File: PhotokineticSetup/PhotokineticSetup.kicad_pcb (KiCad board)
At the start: 2 copper layers, 26 parts, among them J1 Conn_01x02, J2 Serial, J3 LEDs, J4 Switches, J5 Outputs, J6 Inputs, J7 Conn_01x20, J8 Conn_01x20, U1 MAX232, U2 ILD615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

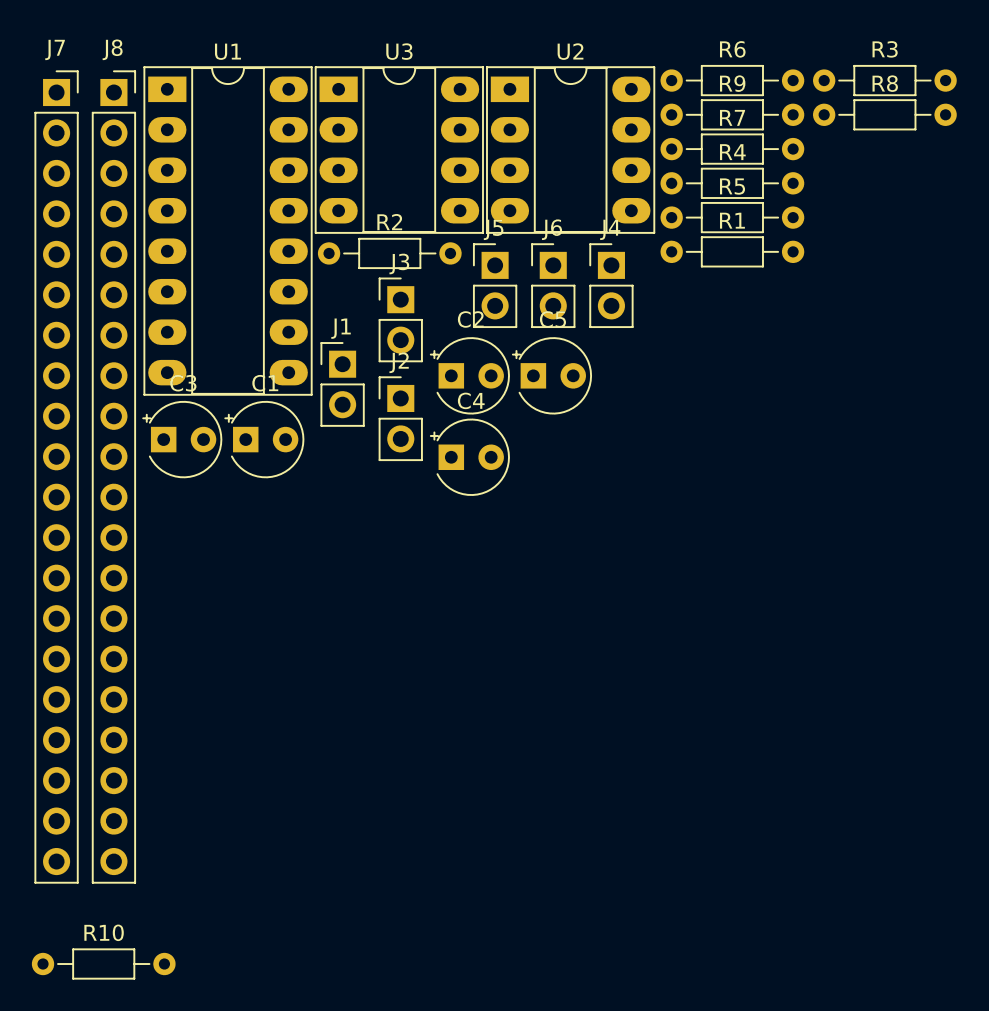
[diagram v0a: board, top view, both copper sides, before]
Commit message: Clearer optocouplers outputs and stronger input
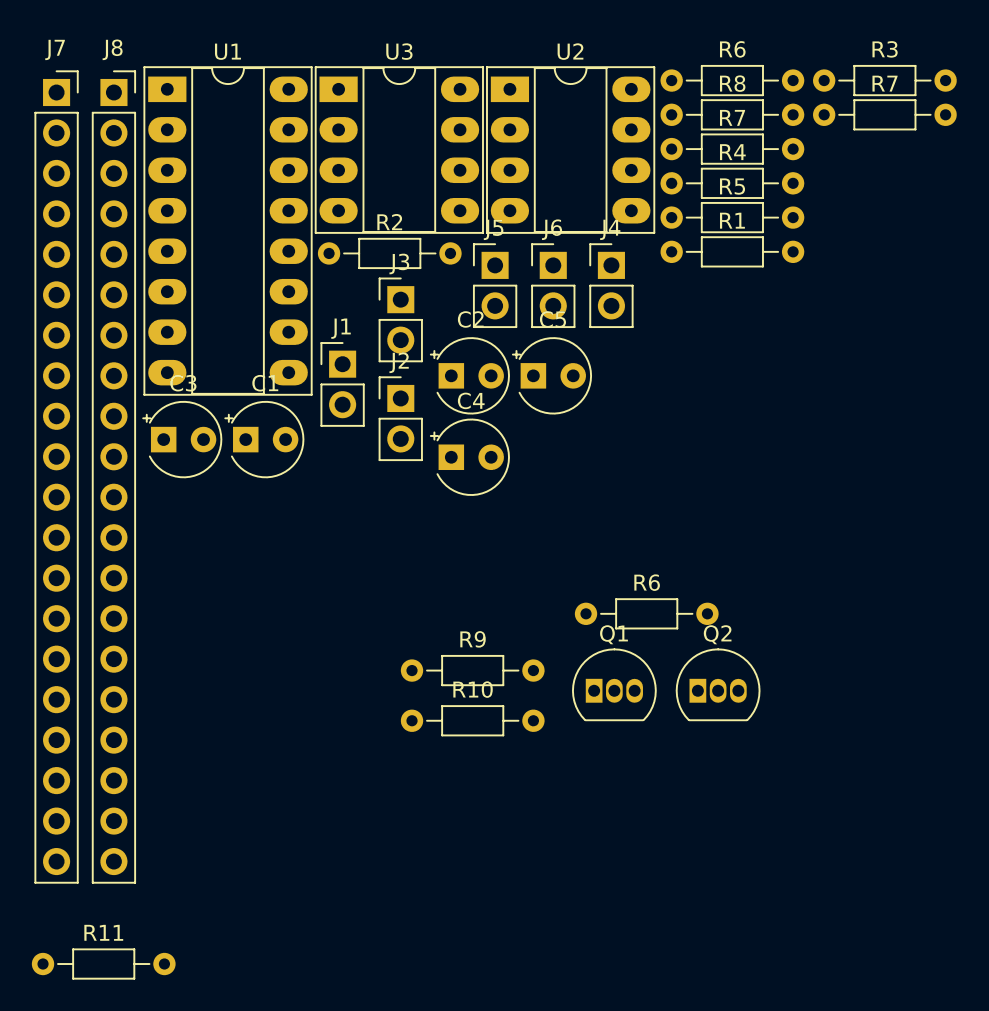
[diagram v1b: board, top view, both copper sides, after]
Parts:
- added Q1: 2N3904, Package_TO_SOT_THT:TO-92_Inline, F.Cu at (124.5, 99.1)
- added Q2: 2N3904, Package_TO_SOT_THT:TO-92_Inline, F.Cu at (131.0, 99.1)
- added R10: 1k, Resistor_THT:R_Axial_DIN0204_L3.6mm_D1.6mm_P7.62mm_Horizontal, F.Cu at (113.0, 100.9)
- added R6: 1k, Resistor_THT:R_Axial_DIN0204_L3.6mm_D1.6mm_P7.62mm_Horizontal, F.Cu at (124.0, 94.2)
- added R9: 1k, Resistor_THT:R_Axial_DIN0204_L3.6mm_D1.6mm_P7.62mm_Horizontal, F.Cu at (113.0, 97.8)
- renumbered R10 to R11, R8 to R7, R9 to R8
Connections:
- J8 pad 13: Net-(J8-Pad13) -> /PA3
- J8 pad 14: Net-(J8-Pad14) -> /PA2
- R5 pad 2: Net-(R5-Pad2) -> Net-(J5-Pad1)
- R7 pad 1: Net-(J6-Pad1) -> +3V3
- R8 pad 1: Net-(J6-Pad2) -> +3V3
- U1 pad 10: Net-(U1-Pad10) -> /PA2
- U1 pad 15: GND -> Net-(U1-Pad15)
- U1 pad 9: Net-(U1-Pad9) -> /PA3
- U2 pad 5: Net-(J5-Pad2) -> GND
- U2 pad 6: Net-(R5-Pad2) -> Net-(J5-Pad2)
- U2 pad 7: Net-(R5-Pad2) -> Net-(J5-Pad1)
- U2 pad 8: Net-(J5-Pad1) -> GND
- U3 pad 2: GND -> Net-(Q1-Pad3)
- U3 pad 3: GND -> Net-(Q2-Pad3)

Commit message: LED resistors calculated according to forward voltage
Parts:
- R1: value 150 -> 82
- R11, R2: value 100 -> 68
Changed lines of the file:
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@@
       (effects (font (size 1 1) (thickness 0.15)))
     )
-    (fp_text value 150 (at 3.81 1.92) (layer F.Fab)
+    (fp_text value 82 (at 3.81 1.92) (layer F.Fab)
       (effects (font (size 1 1) (thickness 0.15)))
     )
@@
       (effects (font (size 1 1) (thickness 0.15)))
     )
-    (fp_text value 100 (at 3.81 1.92) (layer F.Fab)
+    (fp_text value 68 (at 3.81 1.92) (layer F.Fab)
       (effects (font (size 1 1) (thickness 0.15)))
     )
@@
       (effects (font (size 1 1) (thickness 0.15)))
     )
-    (fp_text value 100 (at 3.81 1.92) (layer F.Fab)
-      (effects (font (size 1 1) (thickness 0.15)))
-    )
+    (fp_text value 68 (at 3.81 1.92) (layer F.Fab)
+      (effects (font (size 1 1) (thickness 0.15)))
+    )

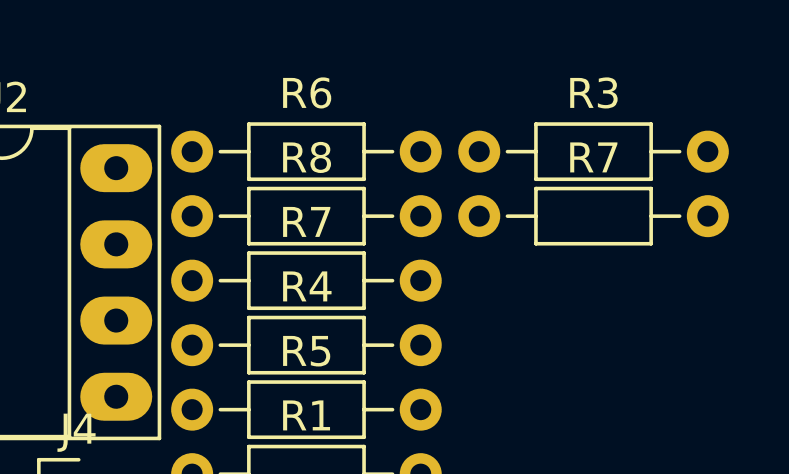
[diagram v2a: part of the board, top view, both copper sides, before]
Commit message: Missing GND node + better placement of R7 & R8
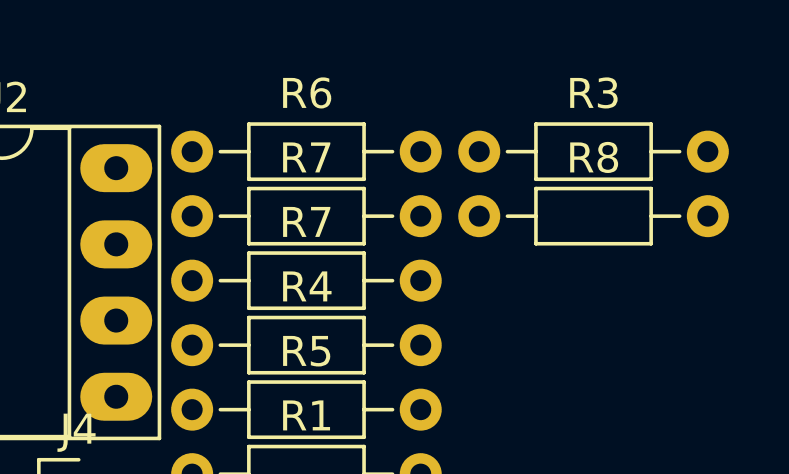
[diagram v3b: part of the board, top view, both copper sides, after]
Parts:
- renumbered R8 to R7, R7 to R8
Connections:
- Q1 pad 1: GND -> Net-(Q1-Pad1)
- Q1 pad 2: Net-(Q1-Pad2) -> Net-(J6-Pad1)
- Q2 pad 1: GND -> Net-(Q2-Pad1)
- Q2 pad 2: Net-(Q2-Pad2) -> Net-(J6-Pad2)
- R7 pad 1: +3V3 -> Net-(Q1-Pad1)
- R7 pad 2: Net-(R8-Pad2) -> GND
- R8 pad 1: +3V3 -> Net-(Q2-Pad1)
- R8 pad 2: Net-(R7-Pad2) -> GND
- U1 pad 15: Net-(U1-Pad15) -> GND
- U3 pad 1: Net-(R7-Pad2) -> +3V3
- U3 pad 4: Net-(R8-Pad2) -> +3V3
